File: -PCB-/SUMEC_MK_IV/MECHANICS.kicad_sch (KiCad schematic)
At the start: 0 parts

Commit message: MK_IV update
Power supp sheet done, mechanical sheet almost done, some changes, updates etc.
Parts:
- added C25: 100nF.en, Capacitor_SMD:C_0805_2012Metric_Pad1.18x1.45mm_HandSolder, symbol Device:C
- added C26: 100nF.boot, Capacitor_SMD:C_0805_2012Metric_Pad1.18x1.45mm_HandSolder, symbol Device:C
- added H1, H2, H3, H4: Mounting Hole M3, MountingHole:MountingHole_3.2mm_M3_Pad_Via, symbol Mechanical:MountingHole_Pad
- added J10, J11: Conn_01x06_Socket, symbol Connector:Conn_01x06_Socket
- added R10: 10k.mcu, Resistor_SMD:R_0805_2012Metric_Pad1.20x1.40mm_HandSolder, symbol Device:R
- added SW2, SW3, SW4, SW5, SW6: SW_Push, Button_Switch_SMD:SW_SPST_B3U-1000P, symbol Switch:SW_Push
- added TP1, TP2, TP3, TP4: TestPoint, TestPoint:TestPoint_Pad_D1.5mm, symbol Connector:TestPoint
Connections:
- new net +3V3: J10.3 (Pin_3), J11.3 (Pin_3), R10.2, SW4.1, SW5.1, SW6.1
- new net BOOT: C26.1, SW3.2
- new net EN: C25.1, R10.1, SW2.2
- new net GND: C25.2, C26.2, H1.1, H2.1, H3.1, H4.1, J10.6 (Pin_6), J11.6 (Pin_6), SW2.1, SW3.1
- new net M1A: J10.1 (Pin_1)
- new net M1B: J10.2 (Pin_2)
- new net M2A: J11.1 (Pin_1)
- new net M2B: J11.2 (Pin_2)
- new net OUT 1A: J10.4 (Pin_4)
- new net OUT 1B: J10.5 (Pin_5)
- new net OUT 2A: J11.4 (Pin_4)
- new net OUT 2B: J11.5 (Pin_5)
- new net TEST PROGRAM: SW4.2
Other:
- note added: "6-pin JST SH-style male connector / encoder motors"
- note added: "ASK NAT - test buttons"
- note added: "BOOT"
- note added: "Buttons for BOOT and ENABLE functions. If the device does not support the auto download mode, you need to get into the download mode manually. To do so, press and hold the BOOT button and then press the RESET button once. After that release the BOOT button."
- note added: "CHECK IF THE MIRRORING IS NECESSARY CHECK CHECK CHECK"
- note added: "CONNECTORS"
- note added: "EN=RESET, BOOT=bootloader mode Enable (EN) is the 3.3V regulator's enable pin. It's pulled up, so connect to ground to disable the 3.3V regulator. This means that you can use this pin connected to a pushbutton to restart your ESP32, for example."
- note added: "ENABLE"
- note added: "M1"
- note added: "M2"
- note added: "M3 Padded Mounting holes Mounting holes that are screwed to the threaded holes on the chassis."
- note added: "MOTORS"
- note added: "MOUNTING HOLES / TEST POINTS"
- note added: "PUSH BUTTONS"

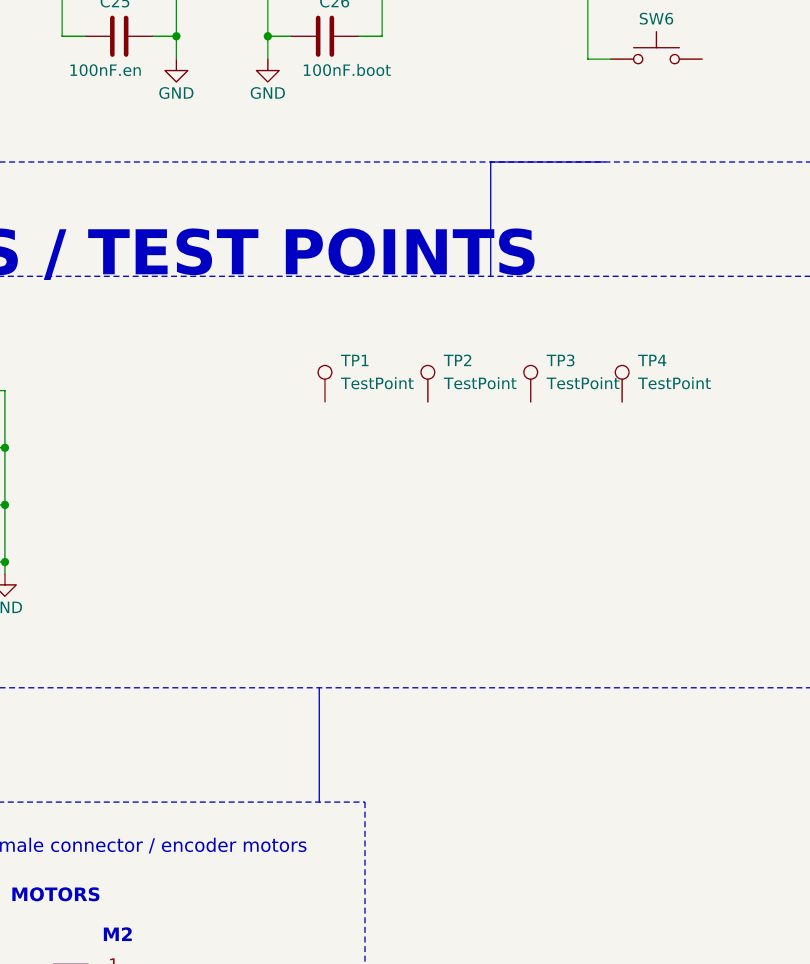
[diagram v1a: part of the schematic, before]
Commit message: MK4 schematic update
Almost done. Did some work on motor drivers, should be final now. Sensors sheet is almost done - object detecting missing. MCU sheet - missing. but yeah. almost done.
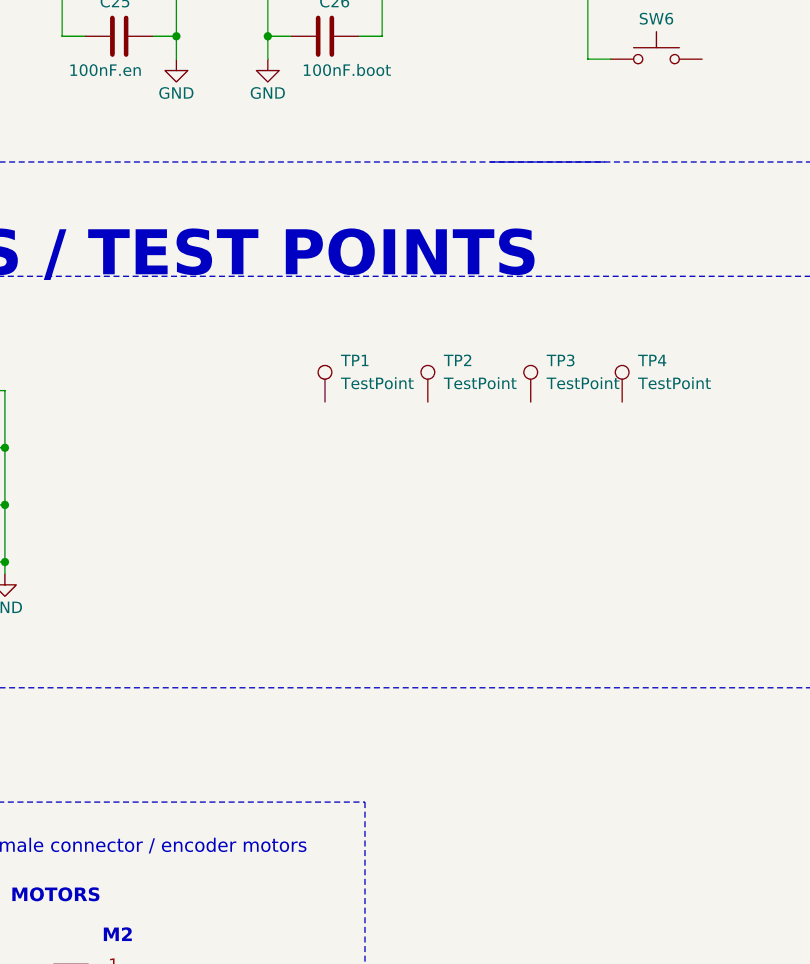
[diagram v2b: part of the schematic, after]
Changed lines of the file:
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@@
 		(color 0 0 0 0)
 	)
+	(wire
+		(pts
+			(xy 144.78 50.8) (xy 149.86 50.8)
+		)
+		(stroke
+			(width 0)
+			(type default)
+		)
+	)
+	(wire
+		(pts
+			(xy 102.87 116.84) (xy 102.87 115.57)
+		)
+		(stroke
+			(width 0)
+			(type default)
+		)
+	)
+	(wire
+		(pts
+			(xy 102.87 96.52) (xy 102.87 102.87)
+		)
+		(stroke
+			(width 0)
+			(type default)
+		)
+	)
+	(wire
+		(pts
+			(xy 88.9 109.22) (xy 102.87 109.22)
+		)
+		(stroke
+			(width 0)
+			(type default)
+		)
+	)
+	(wire
+		(pts
+			(xy 121.92 50.8) (xy 121.92 57.15)
+		)
+		(stroke
+			(width 0)
+			(type default)
+		)
+	)
+	(wire
+		(pts
+			(xy 109.22 46.99) (xy 109.22 50.8)
+		)
+		(stroke
+			(width 0)
+			(type default)
+		)
+	)
+	(wire
+		(pts
+			(xy 102.87 50.8) (xy 109.22 50.8)
+		)
+		(stroke
+			(width 0)
+			(type default)
+		)
+	)
+	(wire
+		(pts
+			(xy 167.64 52.07) (xy 170.18 52.07)
+		)
+		(stroke
+			(width 0)
+			(type default)
+		)
+	)
+	(wire
+		(pts
+			(xy 132.08 59.69) (xy 132.08 57.15)
+		)
+		(stroke
+			(width 0)
+			(type default)
+		)
+	)
+	(wire
+		(pts
+			(xy 121.92 59.69) (xy 121.92 57.15)
+		)
+		(stroke
+			(width 0)
+			(type default)
+		)
+	)
+	(wire
+		(pts
+			(xy 144.78 50.8) (xy 144.78 57.15)
+		)
+		(stroke
+			(width 0)
+			(type default)
+		)
+	)
+	(wire
+		(pts
+			(xy 166.37 44.45) (xy 167.64 44.45)
+		)
+		(stroke
+			(width 0)
+			(type default)
+		)
+	)
+	(wire
+		(pts
+			(xy 170.18 59.69) (xy 167.64 59.69)
+		)
+		(stroke
+			(width 0)
+			(type default)
+		)
+	)
+	(wire
+		(pts
+			(xy 88.9 96.52) (xy 102.87 96.52)
+		)
+		(stroke
+			(width 0)
+			(type default)
+		)
+	)
+	(wire
+		(pts
+			(xy 102.87 109.22) (xy 102.87 115.57)
+		)
+		(stroke
+			(width 0)
+			(type default)
+		)
+	)
+	(wire
+		(pts
+			(xy 110.49 173.99) (xy 113.03 173.99)
+		)
+		(stroke
+			(width 0)
+			(type default)
+		)
+	)
+	(wire
+		(pts
+			(xy 121.92 57.15) (xy 119.38 57.15)
+		)
+		(stroke
+			(width 0)
+			(type default)
+		)
+	)
+	(wire
+		(pts
+			(xy 167.64 44.45) (xy 167.64 52.07)
+		)
+		(stroke
+			(width 0)
+			(type default)
+		)
+	)
+	(wire
+		(pts
+			(xy 102.87 102.87) (xy 102.87 109.22)
+		)
+		(stroke
+			(width 0)
+			(type default)
+		)
+	)
+	(wire
+		(pts
+			(xy 109.22 39.37) (xy 109.22 38.1)
+		)
+		(stroke
+			(width 0)
+			(type default)
+		)
+	)
+	(wire
+		(pts
+			(xy 142.24 57.15) (xy 144.78 57.15)
+		)
+		(stroke
+			(width 0)
+			(type default)
+		)
+	)
+	(wire
+		(pts
+			(xy 132.08 50.8) (xy 132.08 57.15)
+		)
+		(stroke
+			(width 0)
+			(type default)
+		)
+	)
 	(polyline
 		(pts
-			(xy 156.845 71.12) (xy 156.845 83.82)
-		)
-		(stroke
-			(width 0)
-			(type default)
-		)
-	)
-	(wire
-		(pts
-			(xy 144.78 50.8) (xy 149.86 50.8)
-		)
-		(stroke
-			(width 0)
-			(type default)
-		)
-	)
-	(wire
-		(pts
-			(xy 102.87 116.84) (xy 102.87 115.57)
-		)
-		(stroke
-			(width 0)
-			(type default)
-		)
-	)
-	(wire
-		(pts
-			(xy 102.87 96.52) (xy 102.87 102.87)
-		)
-		(stroke
-			(width 0)
-			(type default)
-		)
-	)
-	(wire
-		(pts
-			(xy 88.9 109.22) (xy 102.87 109.22)
-		)
-		(stroke
-			(width 0)
-			(type default)
-		)
-	)
-	(wire
-		(pts
-			(xy 121.92 50.8) (xy 121.92 57.15)
-		)
-		(stroke
-			(width 0)
-			(type default)
-		)
-	)
-	(wire
-		(pts
-			(xy 109.22 46.99) (xy 109.22 50.8)
-		)
-		(stroke
-			(width 0)
-			(type default)
-		)
-	)
-	(wire
-		(pts
-			(xy 102.87 50.8) (xy 109.22 50.8)
-		)
-		(stroke
-			(width 0)
-			(type default)
-		)
-	)
-	(wire
-		(pts
-			(xy 167.64 52.07) (xy 170.18 52.07)
-		)
-		(stroke
-			(width 0)
-			(type default)
-		)
-	)
-	(wire
-		(pts
-			(xy 132.08 59.69) (xy 132.08 57.15)
-		)
-		(stroke
-			(width 0)
-			(type default)
-		)
-	)
-	(wire
-		(pts
-			(xy 121.92 59.69) (xy 121.92 57.15)
-		)
-		(stroke
-			(width 0)
-			(type default)
-		)
-	)
-	(wire
-		(pts
-			(xy 144.78 50.8) (xy 144.78 57.15)
-		)
-		(stroke
-			(width 0)
-			(type default)
-		)
-	)
-	(wire
-		(pts
-			(xy 166.37 44.45) (xy 167.64 44.45)
-		)
-		(stroke
-			(width 0)
-			(type default)
-		)
-	)
-	(wire
-		(pts
-			(xy 170.18 59.69) (xy 167.64 59.69)
-		)
-		(stroke
-			(width 0)
-			(type default)
-		)
-	)
-	(wire
-		(pts
-			(xy 88.9 96.52) (xy 102.87 96.52)
-		)
-		(stroke
-			(width 0)
-			(type default)
-		)
-	)
-	(wire
-		(pts
-			(xy 102.87 109.22) (xy 102.87 115.57)
-		)
-		(stroke
-			(width 0)
-			(type default)
-		)
-	)
-	(wire
-		(pts
-			(xy 110.49 173.99) (xy 113.03 173.99)
-		)
-		(stroke
-			(width 0)
-			(type default)
-		)
-	)
-	(wire
-		(pts
-			(xy 121.92 57.15) (xy 119.38 57.15)
-		)
-		(stroke
-			(width 0)
-			(type default)
-		)
-	)
-	(wire
-		(pts
-			(xy 167.64 44.45) (xy 167.64 52.07)
-		)
-		(stroke
-			(width 0)
-			(type default)
-		)
-	)
-	(wire
-		(pts
-			(xy 102.87 102.87) (xy 102.87 109.22)
-		)
-		(stroke
-			(width 0)
-			(type default)
-		)
-	)
-	(wire
-		(pts
-			(xy 109.22 39.37) (xy 109.22 38.1)
-		)
-		(stroke
-			(width 0)
-			(type default)
-		)
-	)
-	(wire
-		(pts
-			(xy 142.24 57.15) (xy 144.78 57.15)
-		)
-		(stroke
-			(width 0)
-			(type default)
-		)
-	)
-	(wire
-		(pts
-			(xy 132.08 50.8) (xy 132.08 57.15)
-		)
-		(stroke
-			(width 0)
-			(type default)
-		)
-	)
-	(polyline
-		(pts
 			(xy 156.845 71.12) (xy 169.545 71.12)
 		)
 		(stroke
-			(width 0)
-			(type default)
-		)
-	)
-	(polyline
-		(pts
-			(xy 137.795 129.54) (xy 137.795 142.24)
-		)
-		(stroke

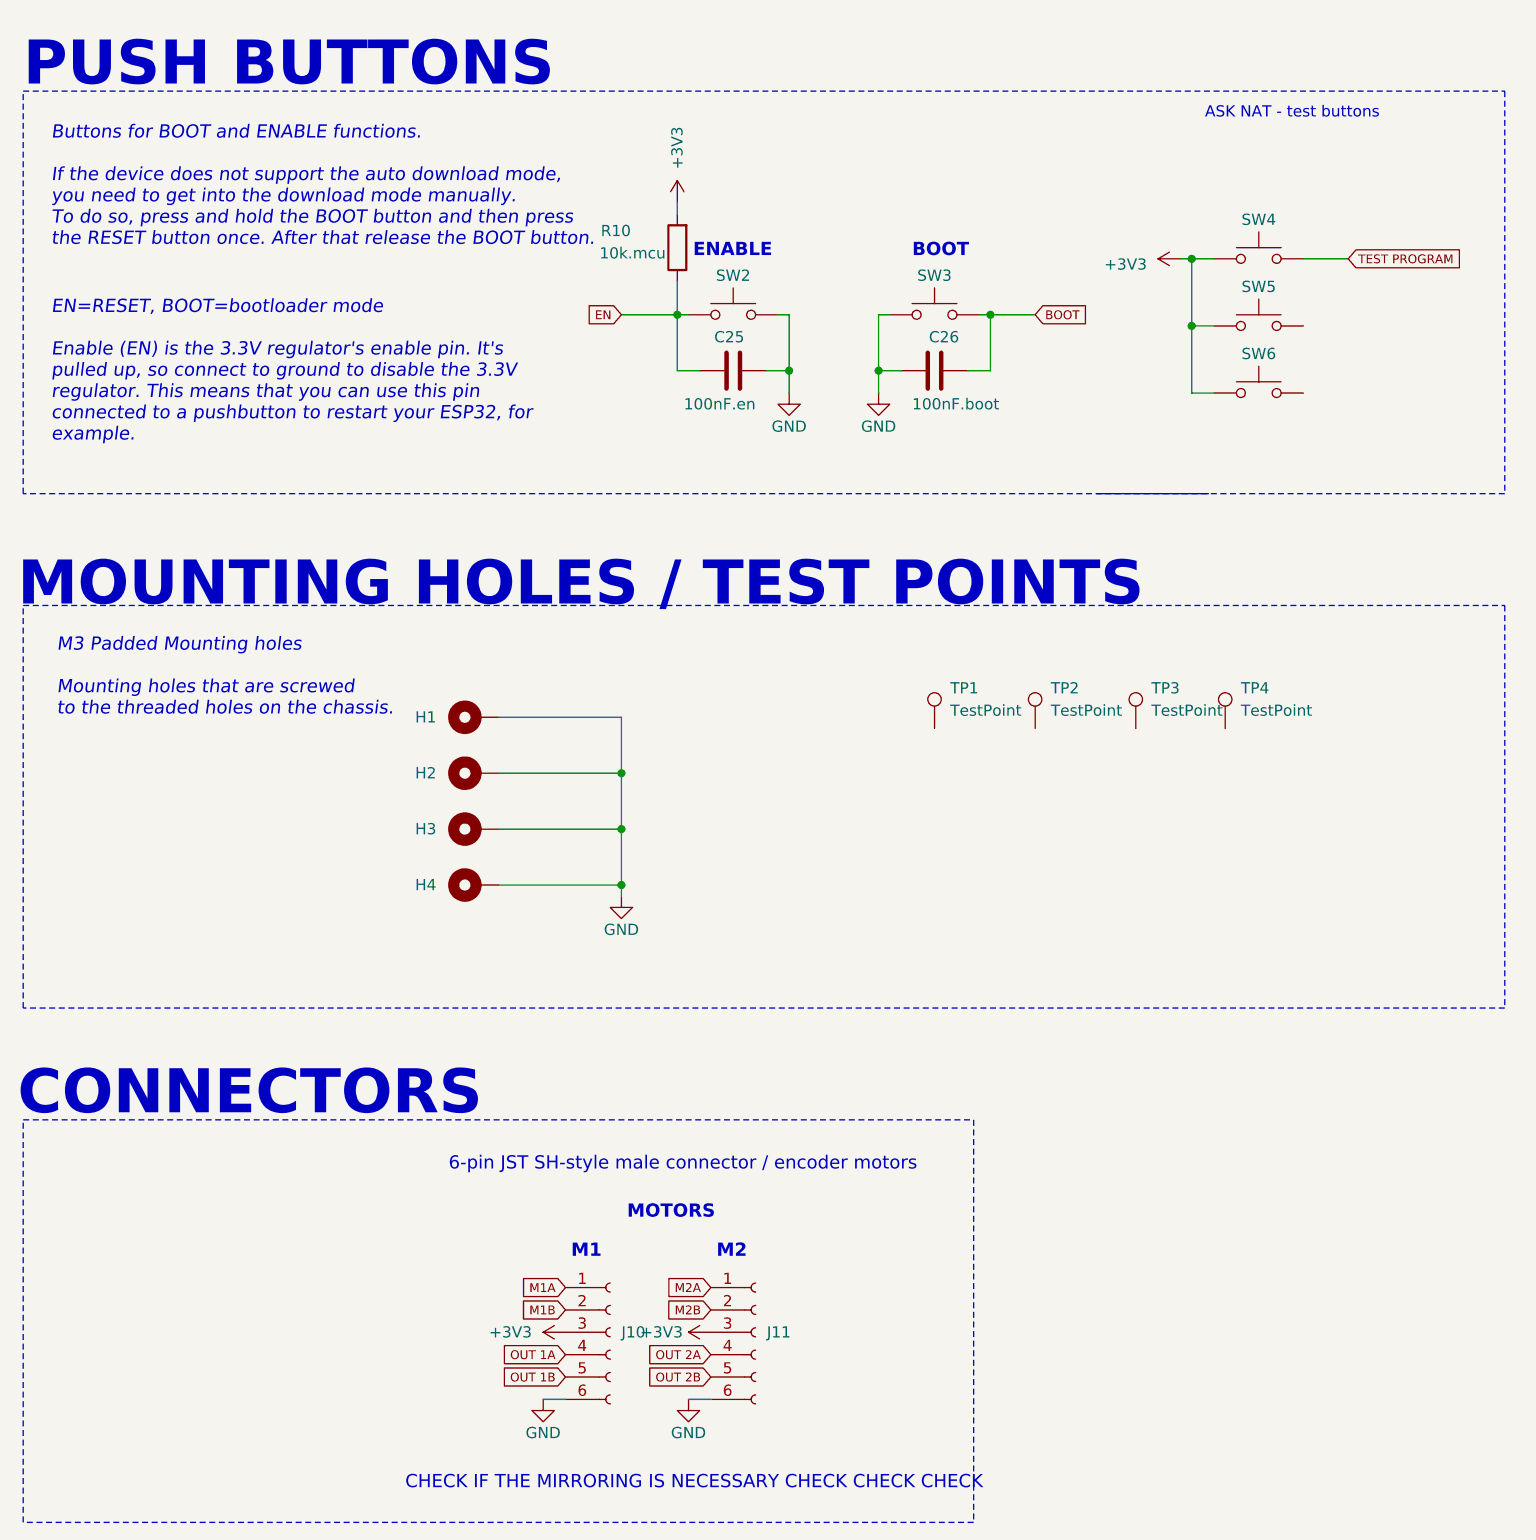
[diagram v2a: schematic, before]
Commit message: MKIV major update
Updated everything, custom symbol for ESP32, MCU sheet done, new test points added, motor control revision.

all left is to clean it up a bit
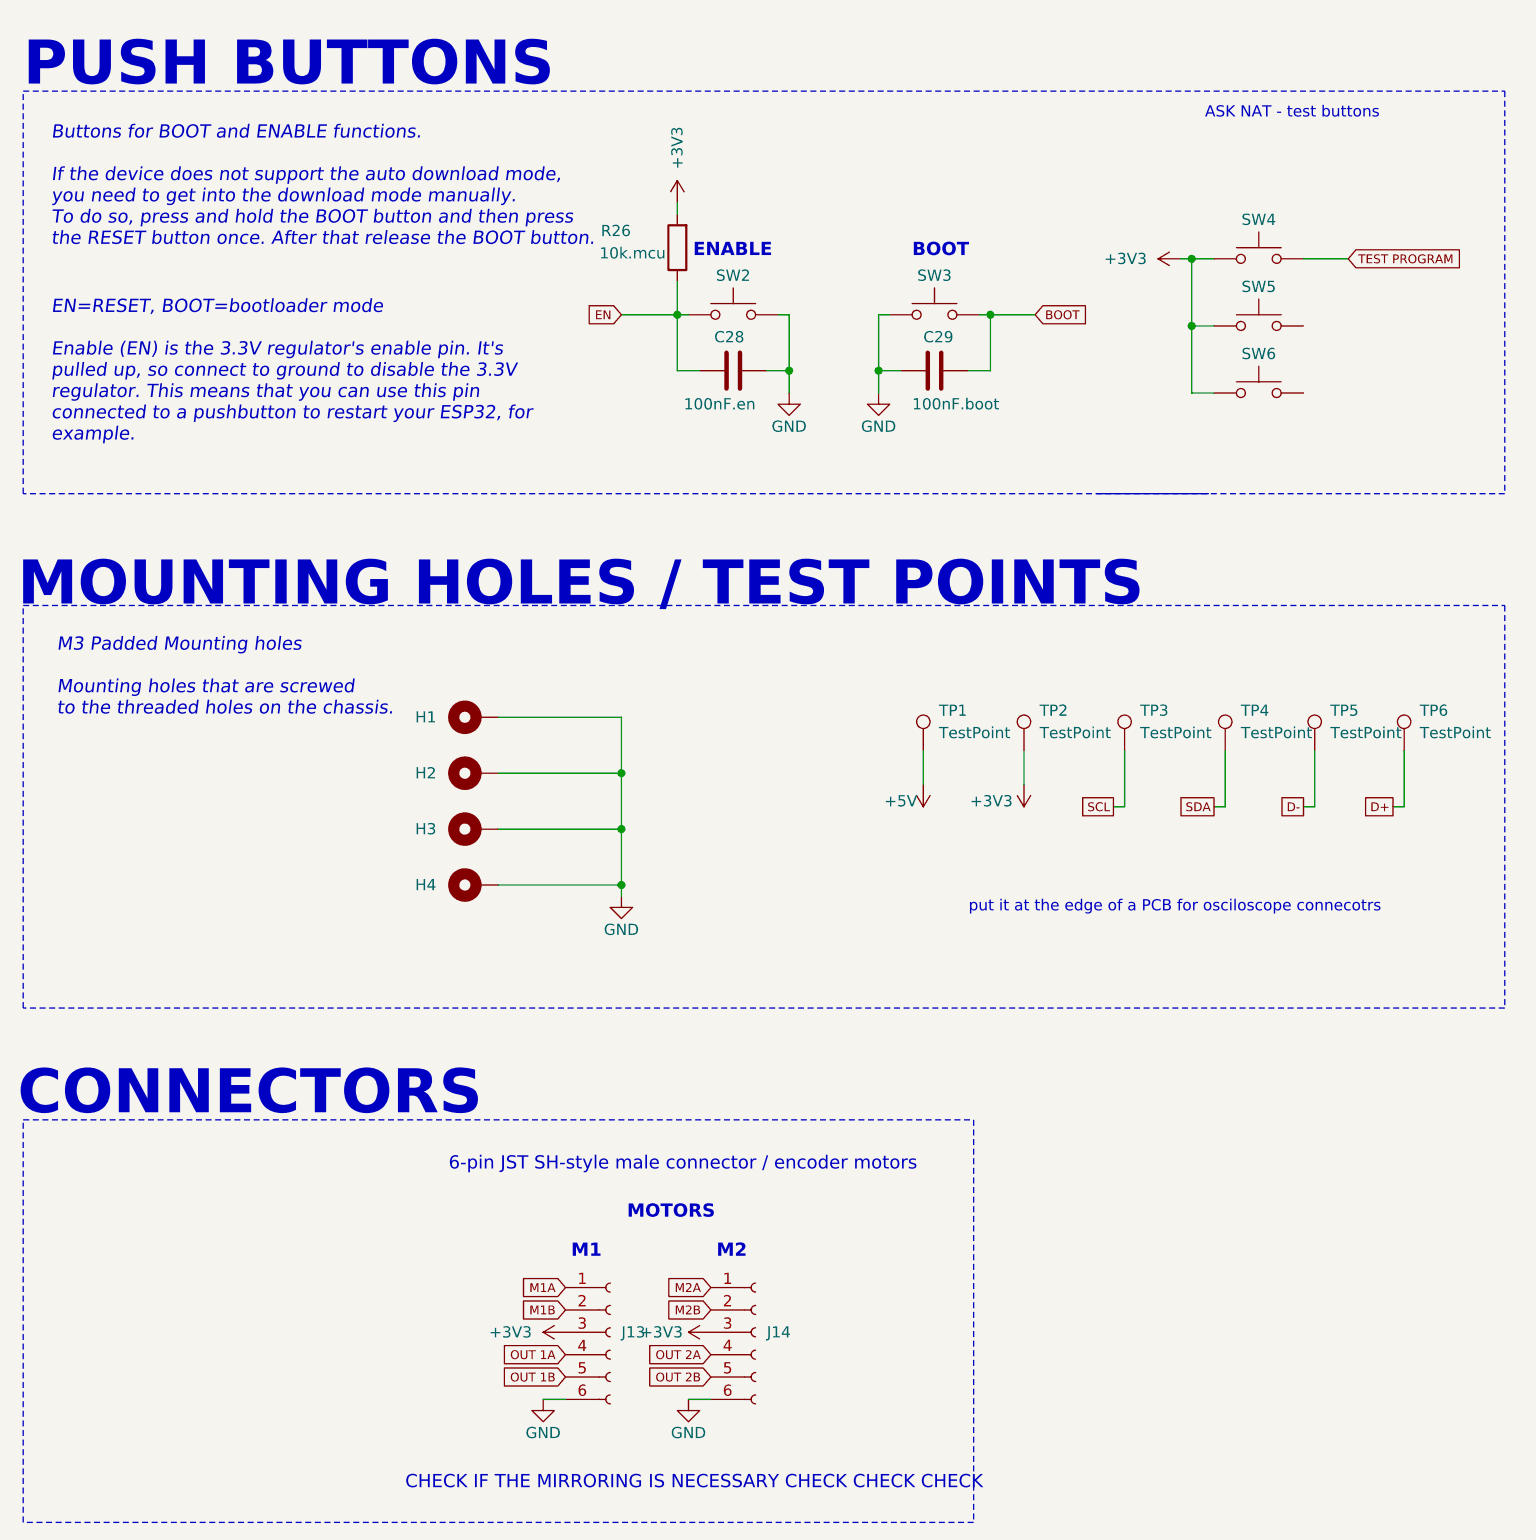
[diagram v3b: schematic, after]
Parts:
- added TP1, TP6: TestPoint, TestPoint:TestPoint_Pad_D1.5mm, symbol Connector:TestPoint
- TP2: renamed from TP1; footprint TestPoint:TestPoint_Pad_D1.5mm -> TestPoint:TestPoint_Loop_D1.80mm_Drill1.0mm_Beaded
- renumbered C25 to C28, C26 to C29, J10 to J13, J11 to J14, R10 to R26, TP2 to TP3, TP3 to TP4, TP4 to TP5
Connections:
- net +3V3: now also TP2.1
- net SDA: now reaches TP4.1
- net SCL: now reaches TP3.1
- net D-: now reaches TP5.1
- new net +5V: TP1.1
- new net D+: TP6.1
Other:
- note added: "put it at the edge of a PCB for osciloscope connecotrs"
- moved on the sheet: TP2, TP3, TP4, TP5
